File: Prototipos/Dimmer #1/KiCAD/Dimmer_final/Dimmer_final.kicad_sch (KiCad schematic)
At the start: 22 parts, among them J2 Conn_01x02, J3 Conn_01x05, K1 SRD-05VDC-SL-C, Q1 BC548B, Q2 BT137, U1 MOC3021M, U2 EL817

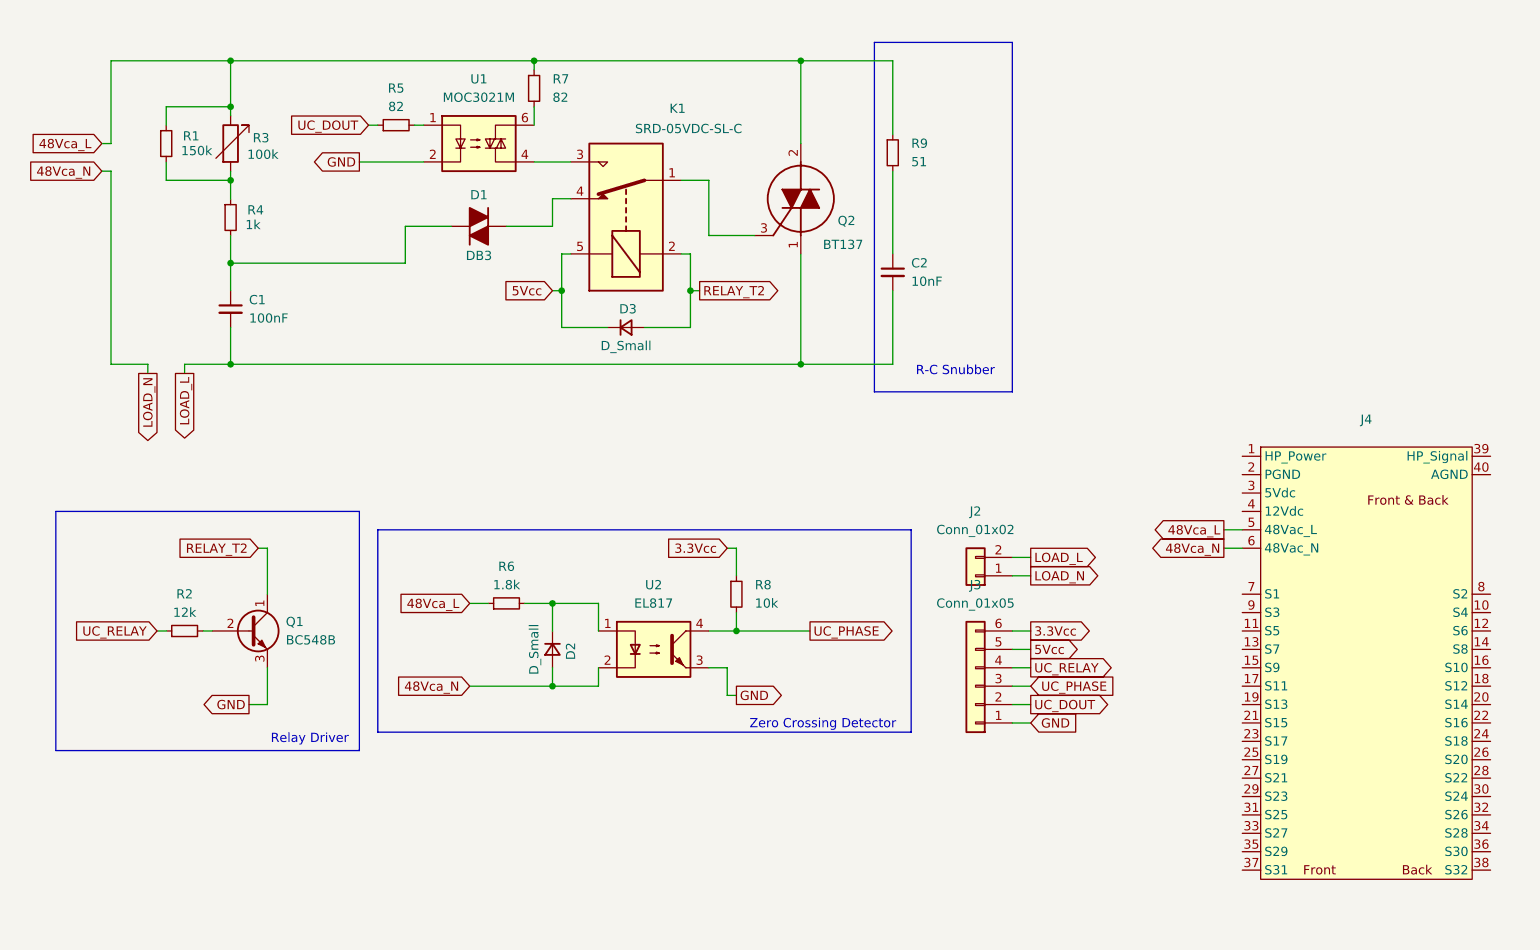
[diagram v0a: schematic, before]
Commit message: Agregar símbolo PCIe
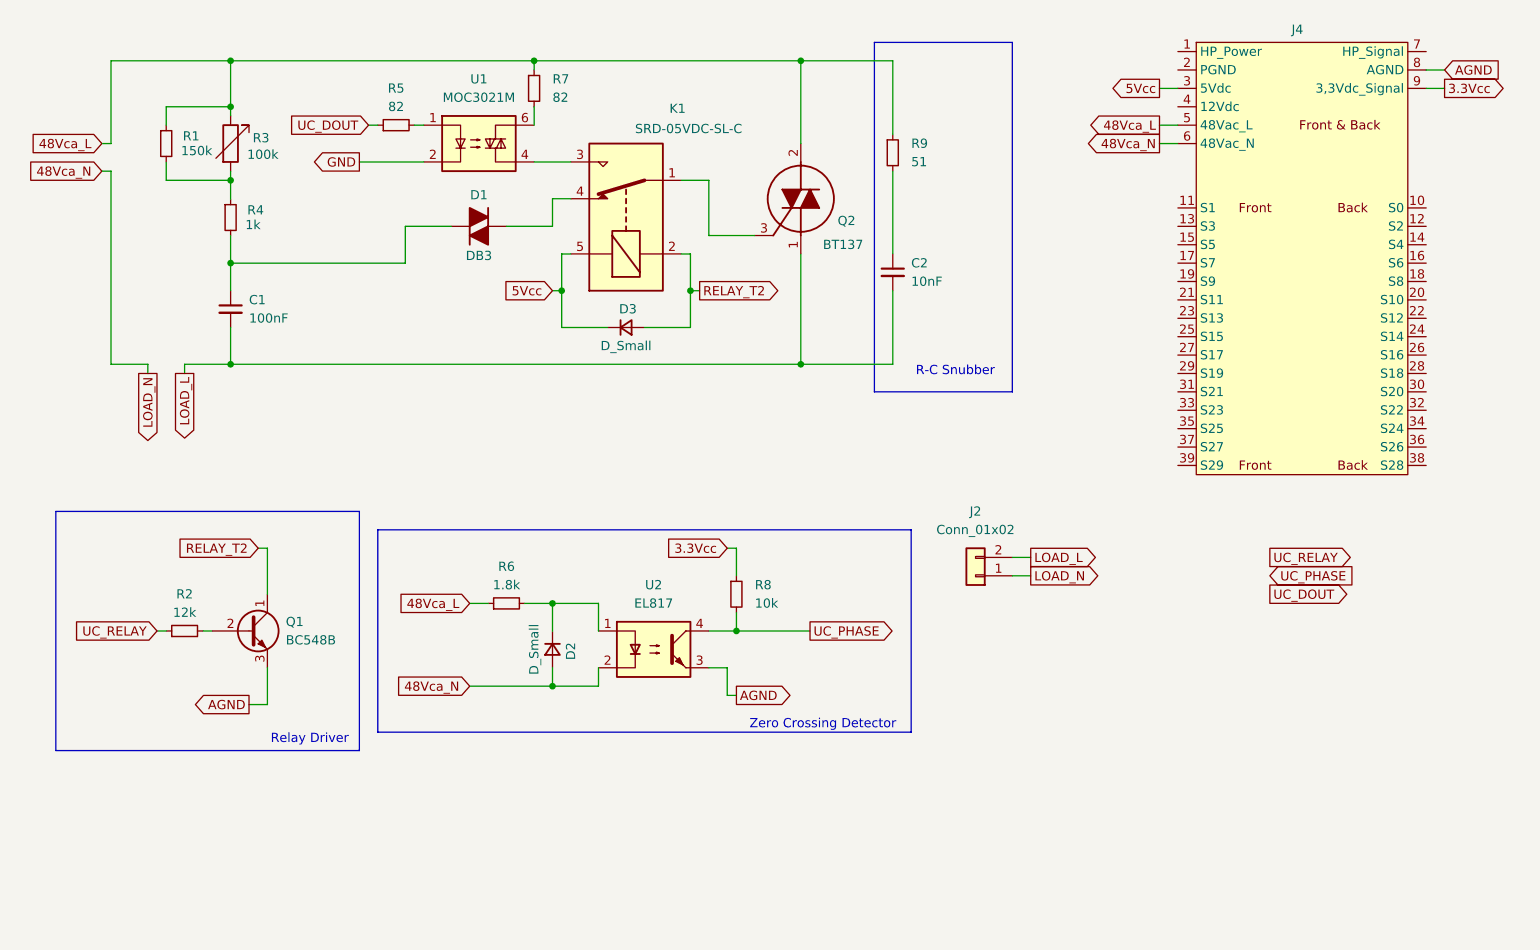
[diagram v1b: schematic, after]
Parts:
- removed J3: Conn_01x05, Connector_PinHeader_2.54mm:PinHeader_1x06_P2.54mm_Vertical, symbol Connector_Generic:Conn_01x06
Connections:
- net 3.3Vcc: now also J4.9 (3,3Vdc_Signal)
- net 5Vcc: now also J4.3 (5Vdc)
- net GND: no longer Q1.3 (E), U2.3
- net AGND: now reaches J4.8 (AGND)
- net AGND: now also Q1.3 (E), U2.3

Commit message: Conectar símbolo PCIe x4, agregar identificación
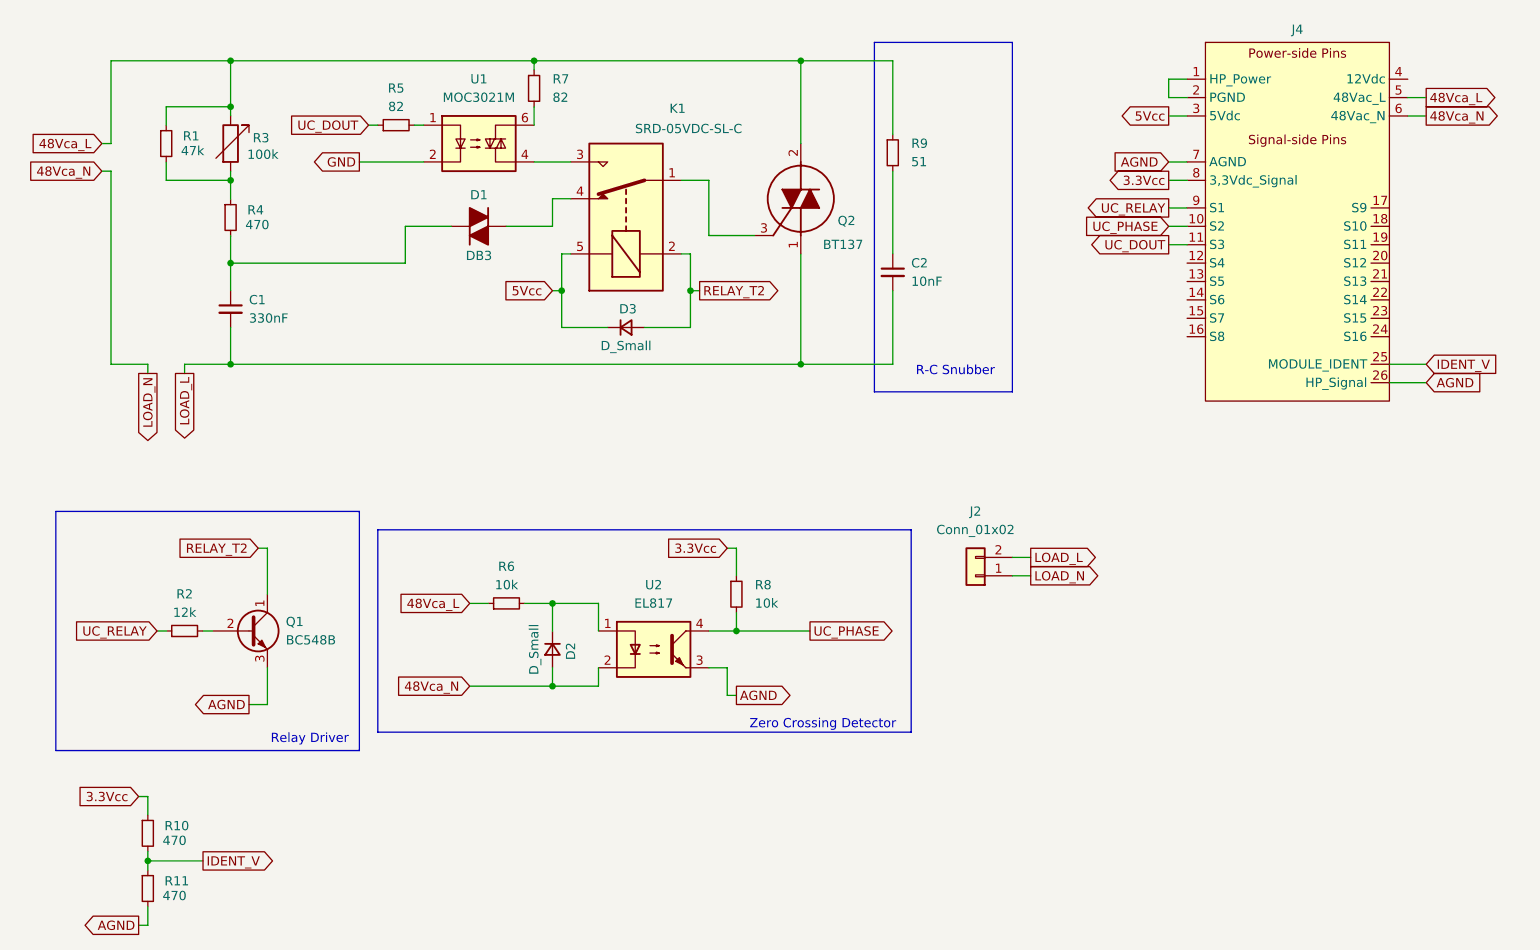
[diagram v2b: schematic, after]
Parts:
- added R10, R11: 470, Resistor_THT:R_Axial_DIN0207_L6.3mm_D2.5mm_P7.62mm_Horizontal, symbol Device:R_Small
- C1: value 100nF -> 330nF
- R1: value 150k -> 47k
- R4: value 1k -> 470
- R6: value 1.8k -> 10k
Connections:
- net 3.3Vcc: now also J4.8 (3,3Vdc_Signal), R10.1; no longer J4.9 (3,3Vdc_Signal)
- net AGND: now also J4.26 (HP_Signal), J4.7 (AGND), R11.2; no longer J4.8 (AGND)
- net UC_DOUT: now also J4.11 (S3)
- net UC_PHASE: now also J4.10 (S2)
- net UC_RELAY: now also J4.9 (S1)
- net at J4.1 (HP_Power): now also J4.2 (PGND)
- net IDENT_V: now reaches J4.25 (MODULE_IDENT)
- net IDENT_V: now also R10.2, R11.1

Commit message: Agregar forma PCB y líneas guía
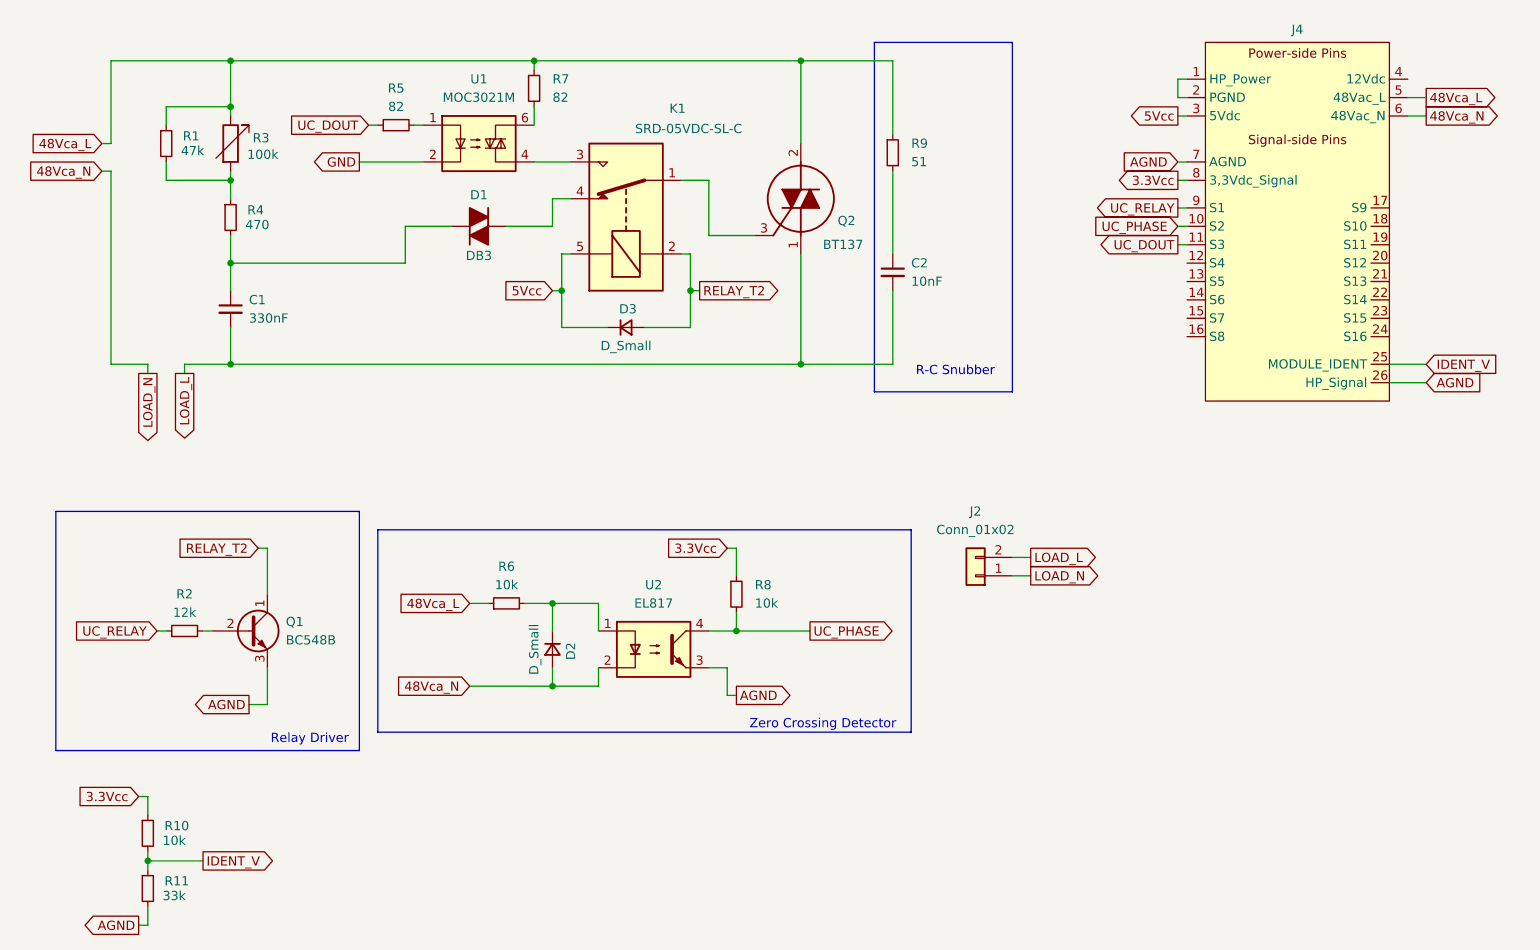
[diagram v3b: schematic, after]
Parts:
- R10: value 470 -> 10k
- R11: value 470 -> 33k
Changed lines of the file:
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@@
 	(wire
 		(pts
-			(xy 195.58 45.72) (xy 193.04 45.72)
+			(xy 195.58 45.72) (xy 194.31 45.72)
 		)
 		(stroke
@@
 	(wire
 		(pts
-			(xy 193.04 45.72) (xy 193.04 43.18)
+			(xy 194.31 45.72) (xy 194.31 43.18)
 		)
 		(stroke
@@
 	(wire
 		(pts
-			(xy 195.58 54.61) (xy 193.04 54.61)
+			(xy 195.58 54.61) (xy 194.31 54.61)
 		)
 		(stroke
@@
 	(wire
 		(pts
-			(xy 193.04 48.26) (xy 195.58 48.26)
+			(xy 194.31 48.26) (xy 195.58 48.26)
 		)
 		(stroke
@@
 	(wire
 		(pts
-			(xy 193.04 43.18) (xy 195.58 43.18)
+			(xy 194.31 43.18) (xy 195.58 43.18)
 		)
 		(stroke
@@
 	(wire
 		(pts
-			(xy 195.58 57.15) (xy 193.04 57.15)
+			(xy 195.58 57.15) (xy 194.31 57.15)
 		)
 		(stroke
@@
 	(wire
 		(pts
-			(xy 193.04 66.04) (xy 195.58 66.04)
+			(xy 194.31 66.04) (xy 195.58 66.04)
 		)
 		(stroke
@@
 	(wire
 		(pts
-			(xy 193.04 60.96) (xy 195.58 60.96)
+			(xy 194.31 60.96) (xy 195.58 60.96)
 		)
 		(stroke
@@
 	(wire
 		(pts
-			(xy 193.04 63.5) (xy 195.58 63.5)
+			(xy 194.31 63.5) (xy 195.58 63.5)
 		)
 		(stroke
@@
 	(global_label "3.3Vcc"
 		(shape output)
-		(at 193.04 57.15 180)
+		(at 194.31 57.15 180)
 		(fields_autoplaced yes)
 		(effects
@@
 		)
 		(property "Intersheetrefs" "${INTERSHEET_REFS}"
-			(at 183.7652 57.15 0)
+			(at 185.0352 57.15 0)
 			(effects
 				(font
@@
 	(global_label "AGND"
 		(shape input)
-		(at 193.04 54.61 180)
+		(at 194.31 54.61 180)
 		(fields_autoplaced yes)
 		(effects
@@
 		)
 		(property "Intersheetrefs" "${INTERSHEET_REFS}"
-			(at 185.0957 54.61 0)
+			(at 186.3657 54.61 0)
 			(effects
 				(font
@@
 	(global_label "UC_RELAY"
 		(shape output)
-		(at 193.04 60.96 180)
+		(at 194.31 60.96 180)
 		(fields_autoplaced yes)
 		(effects
@@
 		)
 		(property "Intersheetrefs" "${INTERSHEET_REFS}"
-			(at 180.8624 60.96 0)
+			(at 182.1324 60.96 0)
 			(effects
 				(font
@@
 	(global_label "UC_PHASE"
 		(shape input)
-		(at 193.04 63.5 180)
+		(at 194.31 63.5 180)
 		(fields_autoplaced yes)
 		(effects
@@
 		)
 		(property "Intersheetrefs" "${INTERSHEET_REFS}"
-			(at 180.4391 63.5 0)
+			(at 181.7091 63.5 0)
 			(effects
 				(font
@@
 	(global_label "5Vcc"
 		(shape output)
-		(at 193.04 48.26 180)
+		(at 194.31 48.26 180)
 		(fields_autoplaced yes)
 		(effects
@@
 		)
 		(property "Intersheetrefs" "${INTERSHEET_REFS}"
-			(at 185.5795 48.26 0)
+			(at 186.8495 48.26 0)
 			(effects
 				(font
@@
 	(global_label "UC_DOUT"
 		(shape output)
-		(at 193.04 66.04 180)
+		(at 194.31 66.04 180)
 		(fields_autoplaced yes)
 		(effects
@@
 		)
 		(property "Intersheetrefs" "${INTERSHEET_REFS}"
-			(at 181.5881 66.04 0)
+			(at 182.8581 66.04 0)
 			(effects
 				(font
@@
 			)
 		)
-		(property "Value" "470"
+		(property "Value" "10k"
 			(at 54.102 148.336 0)
 			(effects
@@
 			)
 		)
-		(property "Value" "470"
+		(property "Value" "33k"
 			(at 54.102 155.956 0)
 			(effects

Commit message: Avances PCB dimmer
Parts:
- J4: footprint (none) -> Proyecto_Final:BUS_PCIE_x4_NSH
- Q2: footprint ProyectoFinal:TO254P470X1000X2000-3P -> Package_TO_SOT_THT:TO-220-3_Horizontal_TabDown
- R3: footprint Potentiometer_THT:Potentiometer_Alps_RK163_Single_Horizontal -> Potentiometer_THT:Potentiometer_Alps_RK09K_Single_Vertical
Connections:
- net GND is gone; now on net AGND: U1.2
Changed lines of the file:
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@@
 	(wire
 		(pts
-			(xy 223.52 85.09) (xy 228.6 85.09)
+			(xy 226.06 82.55) (xy 228.6 82.55)
 		)
 		(stroke
@@
 	(wire
 		(pts
-			(xy 223.52 82.55) (xy 228.6 82.55)
-		)
-		(stroke
-			(width 0)
-			(type default)
-		)
-	)
-	(wire
-		(pts
 			(xy 46.99 55.88) (xy 45.72 55.88)
 		)
@@
 		(pts
 			(xy 129.54 57.15) (xy 125.73 57.15)
+		)
+		(stroke
+			(width 0)
+			(type default)
+		)
+	)
+	(wire
+		(pts
+			(xy 226.06 85.09) (xy 228.6 85.09)
 		)
 		(stroke
@@
 		)
 	)
-	(global_label "GND"
+	(global_label "AGND"
 		(shape output)
 		(at 81.28 54.61 180)
@@
 		)
 		(property "Intersheetrefs" "${INTERSHEET_REFS}"
-			(at 74.4243 54.61 0)
+			(at 73.3357 54.61 0)
 			(effects
 				(font
@@
 			)
 		)
-		(property "Footprint" ""
+		(property "Footprint" "Proyecto_Final:BUS_PCIE_x4_NSH"
 			(at 210.82 62.23 0)
 			(effects
@@
 			)
 		)
-		(property "Footprint" "Potentiometer_THT:Potentiometer_Alps_RK163_Single_Horizontal"
+		(property "Footprint" "Potentiometer_THT:Potentiometer_Alps_RK09K_Single_Vertical"
 			(at 61.722 52.07 90)
 			(effects
@@
 			)
 		)
-		(property "Footprint" "ProyectoFinal:TO254P470X1000X2000-3P"
+		(property "Footprint" "Package_TO_SOT_THT:TO-220-3_Horizontal_TabDown"
 			(at 37.16 66.04 0)
 			(effects

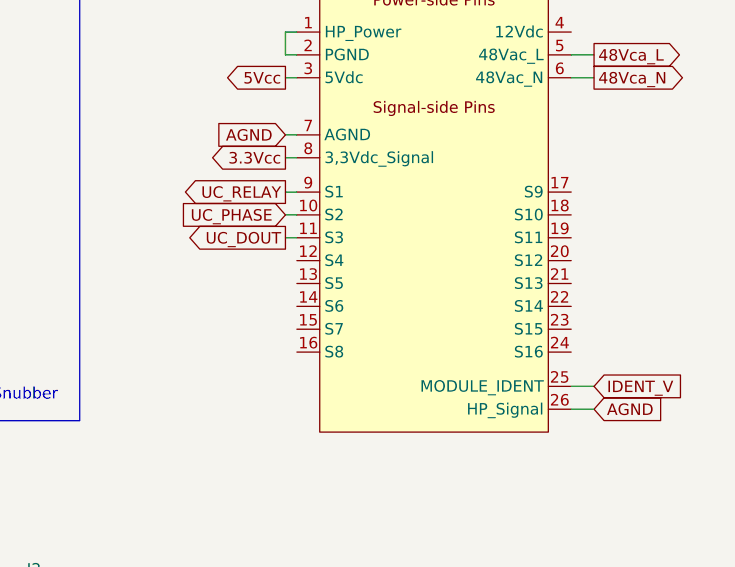
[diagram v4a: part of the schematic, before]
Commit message: Finalizar enrutamiento y primera versión inicial PCB
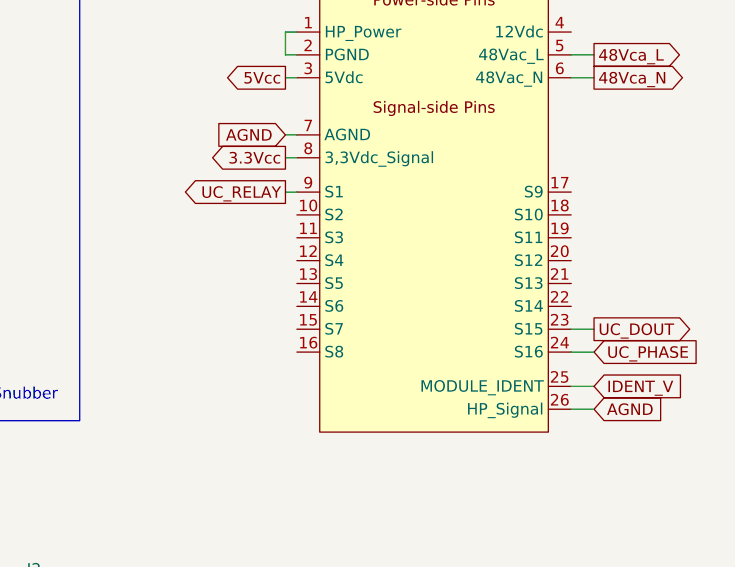
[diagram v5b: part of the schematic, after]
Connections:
- net UC_DOUT: now also J4.23 (S15); no longer J4.11 (S3)
- net UC_PHASE: now also J4.24 (S16); no longer J4.10 (S2)
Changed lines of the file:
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@@
+	(wire
+		(pts
+			(xy 228.6 78.74) (xy 226.06 78.74)
+		)
+		(stroke
+			(width 0)
+			(type default)
+		)
+	)
 	(wire
 		(pts
@@
 	(wire
 		(pts
+			(xy 228.6 76.2) (xy 226.06 76.2)
+		)
+		(stroke
+			(width 0)
+			(type default)
+		)
+	)
+	(wire
+		(pts
 			(xy 194.31 48.26) (xy 195.58 48.26)
 		)
@@
 	(wire
 		(pts
-			(xy 194.31 66.04) (xy 195.58 66.04)
-		)
-		(stroke
-			(width 0)
-			(type default)
-		)
-	)
-	(wire
-		(pts
 			(xy 129.54 57.15) (xy 129.54 64.77)
 		)
@@
 		(pts
 			(xy 127 72.39) (xy 127 77.47)
-		)
-		(stroke
-			(width 0)
-			(type default)
-		)
-	)
-	(wire
-		(pts
-			(xy 194.31 63.5) (xy 195.58 63.5)
 		)
 		(stroke
@@
 	(global_label "UC_PHASE"
 		(shape input)
-		(at 194.31 63.5 180)
-		(fields_autoplaced yes)
-		(effects
-			(font
-				(size 1.27 1.27)
-			)
-			(justify right)
-		)
-		(property "Intersheetrefs" "${INTERSHEET_REFS}"
-			(at 181.7091 63.5 0)
-			(effects
-				(font
-					(size 1.27 1.27)
-				)
-				(justify right)
+		(at 228.6 78.74 0)
+		(fields_autoplaced yes)
+		(effects
+			(font
+				(size 1.27 1.27)
+			)
+			(justify left)
+		)
+		(property "Intersheetrefs" "${INTERSHEET_REFS}"
+			(at 241.2009 78.74 0)
+			(effects
+				(font
+					(size 1.27 1.27)
+				)
+				(justify left)
 				(hide yes)
 			)
@@
 	(global_label "UC_DOUT"
 		(shape output)
-		(at 194.31 66.04 180)
-		(fields_autoplaced yes)
-		(effects
-			(font
-				(size 1.27 1.27)
-			)
-			(justify right)
-		)
-		(property "Intersheetrefs" "${INTERSHEET_REFS}"
-			(at 182.8581 66.04 0)
-			(effects
-				(font
-					(size 1.27 1.27)
-				)
-				(justify right)
-				(hide yes)
-			)
+		(at 228.6 76.2 0)
+		(fields_autoplaced yes)
+		(effects
+			(font
+				(size 1.27 1.27)
+			)
+			(justify left)
+		)
+		(property "Intersheetrefs" "${INTERSHEET_REFS}"
+			(at 240.0519 76.2 0)
+			(effects
+				(font
+					(size 1.27 1.27)
+				)
+				(justify left)
+				(hide yes)
+			)
